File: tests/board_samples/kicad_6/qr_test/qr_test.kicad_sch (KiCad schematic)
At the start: 0 parts

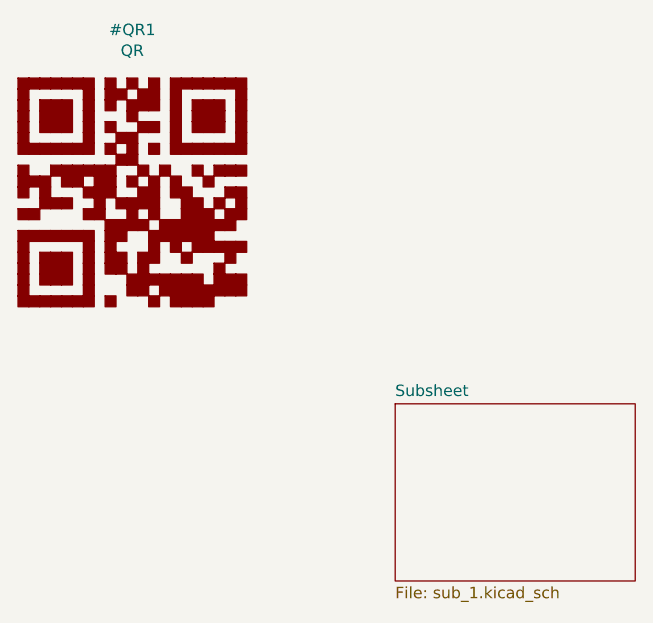
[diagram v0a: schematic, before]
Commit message: Added support for KiCad 6 to the `update_qr` preflight.
Related to #93
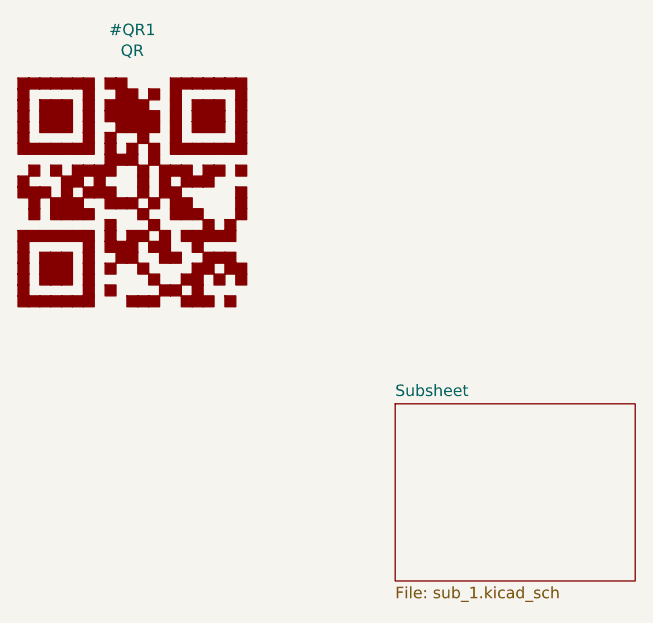
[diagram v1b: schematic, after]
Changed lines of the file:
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@@
-(kicad_sch (version 20211123) (generator eeschema)
+(kicad_sch (version 20211123)
+  (generator eeschema)
   (paper "A4")
-  (title_block
-    (title "QR Test")
+  (title_block (title "QR Test")
     (rev "A")
   )
-  (symbol (lib_id "qr:QR") (at 31.75 39.37 0) (unit 1)
-    (in_bom yes) (on_board yes)
+  (symbol (lib_id "qr:QR")
+    (at 31.75 39.37 0)
+    (unit 1)
+    (in_bom yes)
+    (on_board yes)
     (property "Reference" "#QR1" (id 0) (at 31.75 21.3106 0))
     (property "Value" "QR" (id 1) (at 31.75 23.622 0))
-    (property "Footprint" "QR:QR" (id 2) (at 31.75 35.56 0)
-      (effects (font (size 1.27 1.27)) hide)
-    )
-    (property "Datasheet" "" (id 3) (at 31.75 39.37 0)
-      (effects (font (size 1.27 1.27)) hide)
-    )
-    (property "qr_version" "1" (id 4) (at 31.75 39.37 0)
-      (effects (font (size 1.27 1.27)) hide)
-    )
-    (property "qr_size" "21" (id 5) (at 31.75 39.37 0)
-      (effects (font (size 1.27 1.27)) hide)
-    )
-    (property "qr_ecc" "1,0" (id 6) (at 31.75 39.37 0)
-      (effects (font (size 1.27 1.27)) hide)
-    )
-    (property "qr_mask" "6" (id 7) (at 31.75 39.37 0)
-      (effects (font (size 1.27 1.27)) hide)
-    )
-    (property "qr_text" "bogus 1 2 3 4" (id 8) (at 31.75 39.37 0)
-      (effects (font (size 1.27 1.27)) hide)
-    )
+    (property "Footprint" "QR:QR" (id 2) (at 31.75 35.56 0) (effects (font (size 1.27 1.27)) hide))
+    (property "Datasheet" "" (id 3) (at 31.75 39.37 0) (effects (font (size 1.27 1.27)) hide))
+    (property "qr_version" "1" (id 4) (at 31.75 39.37 0) (effects (font (size 1.27 1.27)) hide))
+    (property "qr_size" "21" (id 5) (at 31.75 39.37 0) (effects (font (size 1.27 1.27)) hide))
+    (property "qr_ecc" "1,0" (id 6) (at 31.75 39.37 0) (effects (font (size 1.27 1.27)) hide))
+    (property "qr_mask" "6" (id 7) (at 31.75 39.37 0) (effects (font (size 1.27 1.27)) hide))
+    (property "qr_text" "bogus 1 2 3 4" (id 8) (at 31.75 39.37 0) (effects (font (size 1.27 1.27)) hide))
   )
-  (sheet (at 60.96 62.865) (size 26.67 19.685) (fields_autoplaced)
+  (sheet (at 60.96 62.865)
+    (size 26.67 19.685)
+    (fields_autoplaced)
     (stroke (width 0) (type solid) (color 0 0 0 0))
-    (fill (color 0 0 0 0.0000))
-    (property "Sheet name" "Subsheet" (id 0) (at 60.96 62.1534 0)
-      (effects (font (size 1.27 1.27)) (justify left bottom))
-    )
-    (property "Sheet file" "sub_1.kicad_sch" (id 1) (at 60.96 83.1346 0)
-      (effects (font (size 1.27 1.27)) (justify left top))
-    )
+    (fill (color 0 0 0 0.0))
+    (property "Sheet name" "Subsheet" (id 0) (at 60.96 62.1534 0) (effects (font (size 1.27 1.27)) (justify left bottom)))
+    (property "Sheet file" "sub_1.kicad_sch" (id 1) (at 60.96 83.1346 0) (effects (font (size 1.27 1.27)) (justify left top)))
   )
-  (sheet_instances
-    (path "/" (page "1"))
+  (sheet_instances (path "/" (page "1"))
     (path "/00000000-0000-0000-0000-000061d2163a" (page "2"))
   )
-  (symbol_instances
-    (path "/00000000-0000-0000-0000-000061d2093f"
-      (reference "#QR1") (unit 1) (value "QR") (footprint "QR:QR")
-    )
-    (path "/00000000-0000-0000-0000-000061d2163a/00000000-0000-0000-0000-000061d3091b"
-      (reference "#QR2") (unit 1) (value "QR2") (footprint "QR:QR2")
-    )
+  (symbol_instances (path "/00000000-0000-0000-0000-000061d2093f" (reference "#QR1") (unit 1) (value "QR") (footprint "QR:QR"))
+    (path "/00000000-0000-0000-0000-000061d2163a/00000000-0000-0000-0000-000061d3091b" (reference "#QR2") (unit 1) (value "QR2") (footprint "QR:QR2"))
   )
 )
